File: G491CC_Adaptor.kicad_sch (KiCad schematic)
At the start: 26 parts, among them J1 Conn_01x12, J2 Conn_01x11, J3 Conn_01x11, J4 Conn_01x12, U1 STM32G491CCUx, U2 AP7343D-33W5, U3 TCR2EE33, Y1 ECX-1637B2 [10pF, 20MHz]

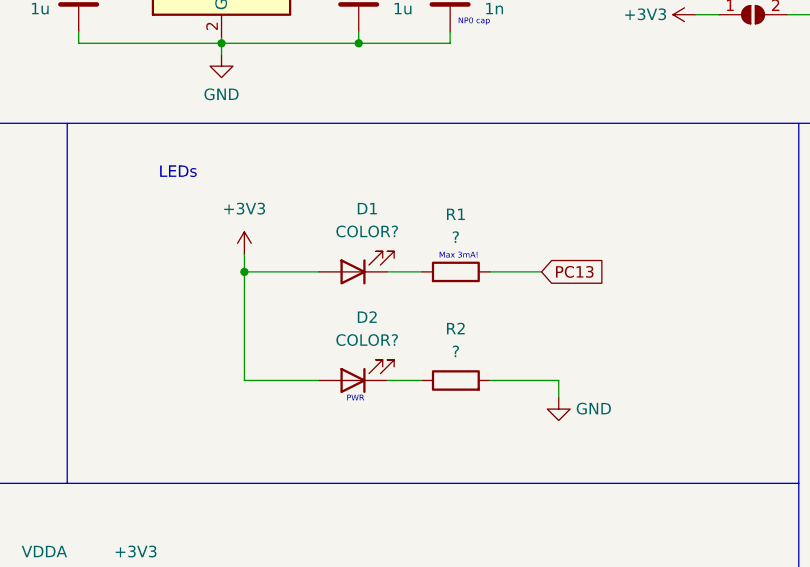
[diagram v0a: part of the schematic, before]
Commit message: LED resistor values
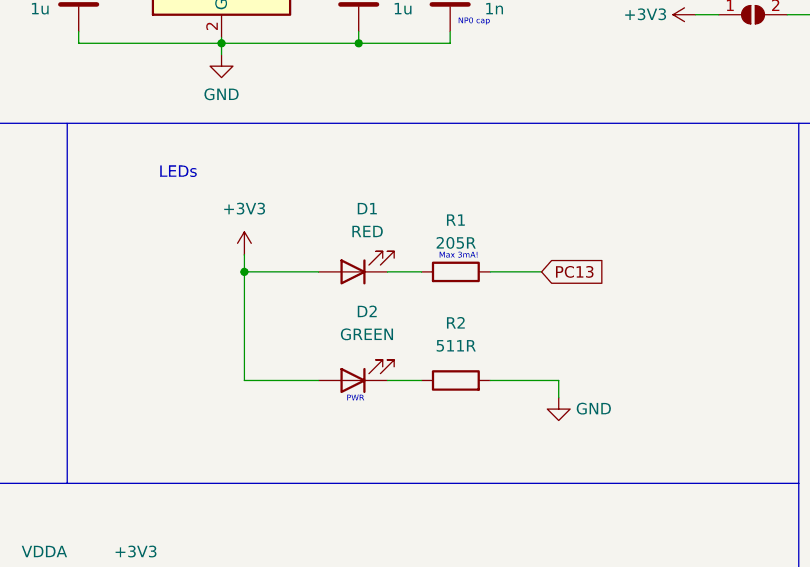
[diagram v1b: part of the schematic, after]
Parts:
- D1: value COLOR? -> RED
- D2: value COLOR? -> GREEN
- R1: value ? -> 205R
- R2: value ? -> 511R
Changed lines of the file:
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@@
     (in_bom yes) (on_board yes) (fields_autoplaced)
     (property "Reference" "D1" (id 0) (at 129.2225 59.69 0))
-    (property "Value" "COLOR?" (id 1) (at 129.2225 62.23 0))
+    (property "Value" "RED" (id 1) (at 129.2225 62.23 0))
     (property "Footprint" "LED_SMD:LED_0603_1608Metric" (id 2) (at 127.635 66.675 0)
       (effects (font (size 1.27 1.27)) hide)
@@
   (symbol (lib_id "Device:LED") (at 127.635 78.74 180) (unit 1)
     (in_bom yes) (on_board yes) (fields_autoplaced)
-    (property "Reference" "D2" (id 0) (at 129.2225 71.755 0))
-    (property "Value" "COLOR?" (id 1) (at 129.2225 74.295 0))
+    (property "Reference" "D2" (id 0) (at 129.2225 71.12 0))
+    (property "Value" "GREEN" (id 1) (at 129.2225 73.66 0))
     (property "Footprint" "LED_SMD:LED_0603_1608Metric" (id 2) (at 127.635 78.74 0)
       (effects (font (size 1.27 1.27)) hide)
@@
   (symbol (lib_id "Device:R") (at 139.065 66.675 270) (mirror x) (unit 1)
     (in_bom yes) (on_board yes) (fields_autoplaced)
-    (property "Reference" "R1" (id 0) (at 139.065 60.325 90))
-    (property "Value" "?" (id 1) (at 139.065 62.865 90))
+    (property "Reference" "R1" (id 0) (at 139.065 60.96 90))
+    (property "Value" "205R" (id 1) (at 139.065 63.5 90))
     (property "Footprint" "Resistor_SMD:R_0603_1608Metric" (id 2) (at 139.065 68.453 90)
       (effects (font (size 1.27 1.27)) hide)
@@
   (symbol (lib_id "Device:R") (at 139.065 78.74 90) (unit 1)
     (in_bom yes) (on_board yes) (fields_autoplaced)
-    (property "Reference" "R2" (id 0) (at 139.065 73.025 90))
-    (property "Value" "?" (id 1) (at 139.065 75.565 90))
+    (property "Reference" "R2" (id 0) (at 139.065 72.39 90))
+    (property "Value" "511R" (id 1) (at 139.065 74.93 90))
     (property "Footprint" "Resistor_SMD:R_0603_1608Metric" (id 2) (at 139.065 80.518 90)
       (effects (font (size 1.27 1.27)) hide)
@@
     )
     (path "/5822aa90-037f-4df2-8d43-45571735352d"
-      (reference "D1") (unit 1) (value "COLOR?") (footprint "LED_SMD:LED_0603_1608Metric")
+      (reference "D1") (unit 1) (value "RED") (footprint "LED_SMD:LED_0603_1608Metric")
     )
     (path "/6b9495a4-4ea3-4c03-a89d-d442a3976e2f"
-      (reference "D2") (unit 1) (value "COLOR?") (footprint "LED_SMD:LED_0603_1608Metric")
+      (reference "D2") (unit 1) (value "GREEN") (footprint "LED_SMD:LED_0603_1608Metric")
     )
     (path "/fac51eb5-6c22-49fe-b812-c82cdf4a6354"
@@
     )
     (path "/8deb6ae7-380c-46f9-8118-56e612f6bc33"
-      (reference "R1") (unit 1) (value "?") (footprint "Resistor_SMD:R_0603_1608Metric")
+      (reference "R1") (unit 1) (value "205R") (footprint "Resistor_SMD:R_0603_1608Metric")
     )
     (path "/ee5b92c3-f274-4fb1-a8f4-38f84016d65a"
-      (reference "R2") (unit 1) (value "?") (footprint "Resistor_SMD:R_0603_1608Metric")
+      (reference "R2") (unit 1) (value "511R") (footprint "Resistor_SMD:R_0603_1608Metric")
     )
     (path "/75e8f134-2388-4bf1-949a-238f84203020"
